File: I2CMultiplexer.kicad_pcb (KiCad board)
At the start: 2 copper layers, 165.1 x 88.9 mm, 178 parts, among them J1 M3, J10 I2C, J11 I2C, J12 I2C, J13 RSS232Out, J14 RSS232In, J15 SPI, J16 SPI, J17 V_{IN}, J18 UART8, J19 UART5, J2 M3, J20 UART6, J3 M3, J4 M3, J5 I2C, J6 I2C, J7 I2C, J8 I2C, J9 I2C, Q1 Q_PMOS_GSD, Q2 Q_PMOS_GSD, U1 Teensy4.1, U2 TCA9548APWR, U3 PCF8574TS, U4 MAX3232, U5 FM24CL16B

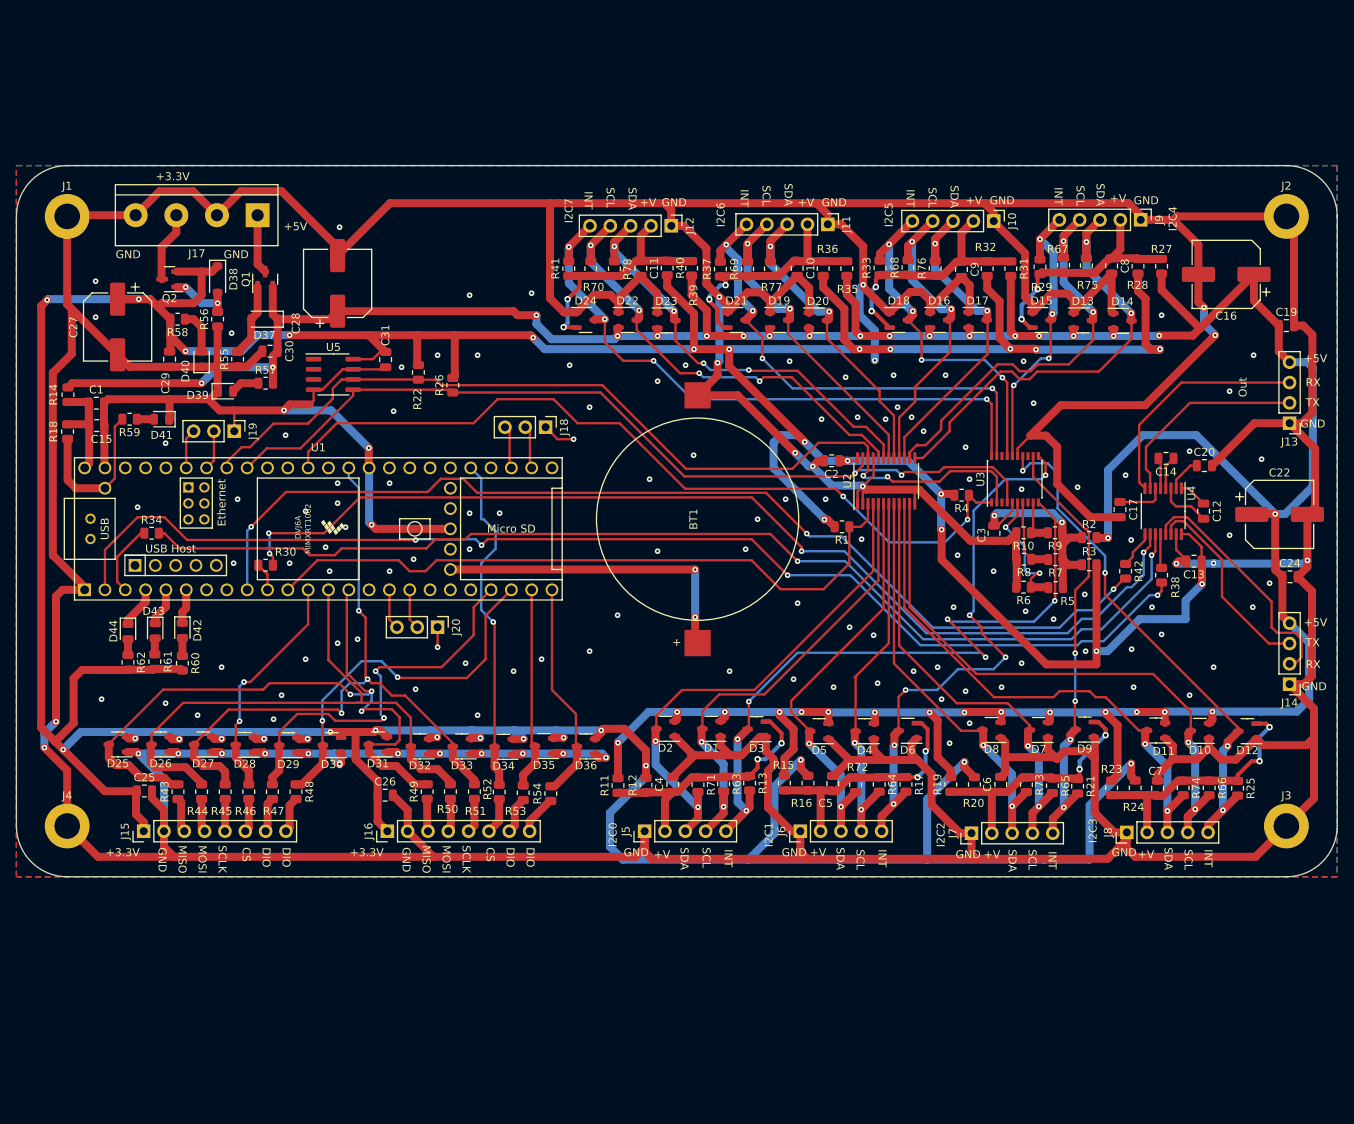
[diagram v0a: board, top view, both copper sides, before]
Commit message: Start layout. Swap side for connectors.
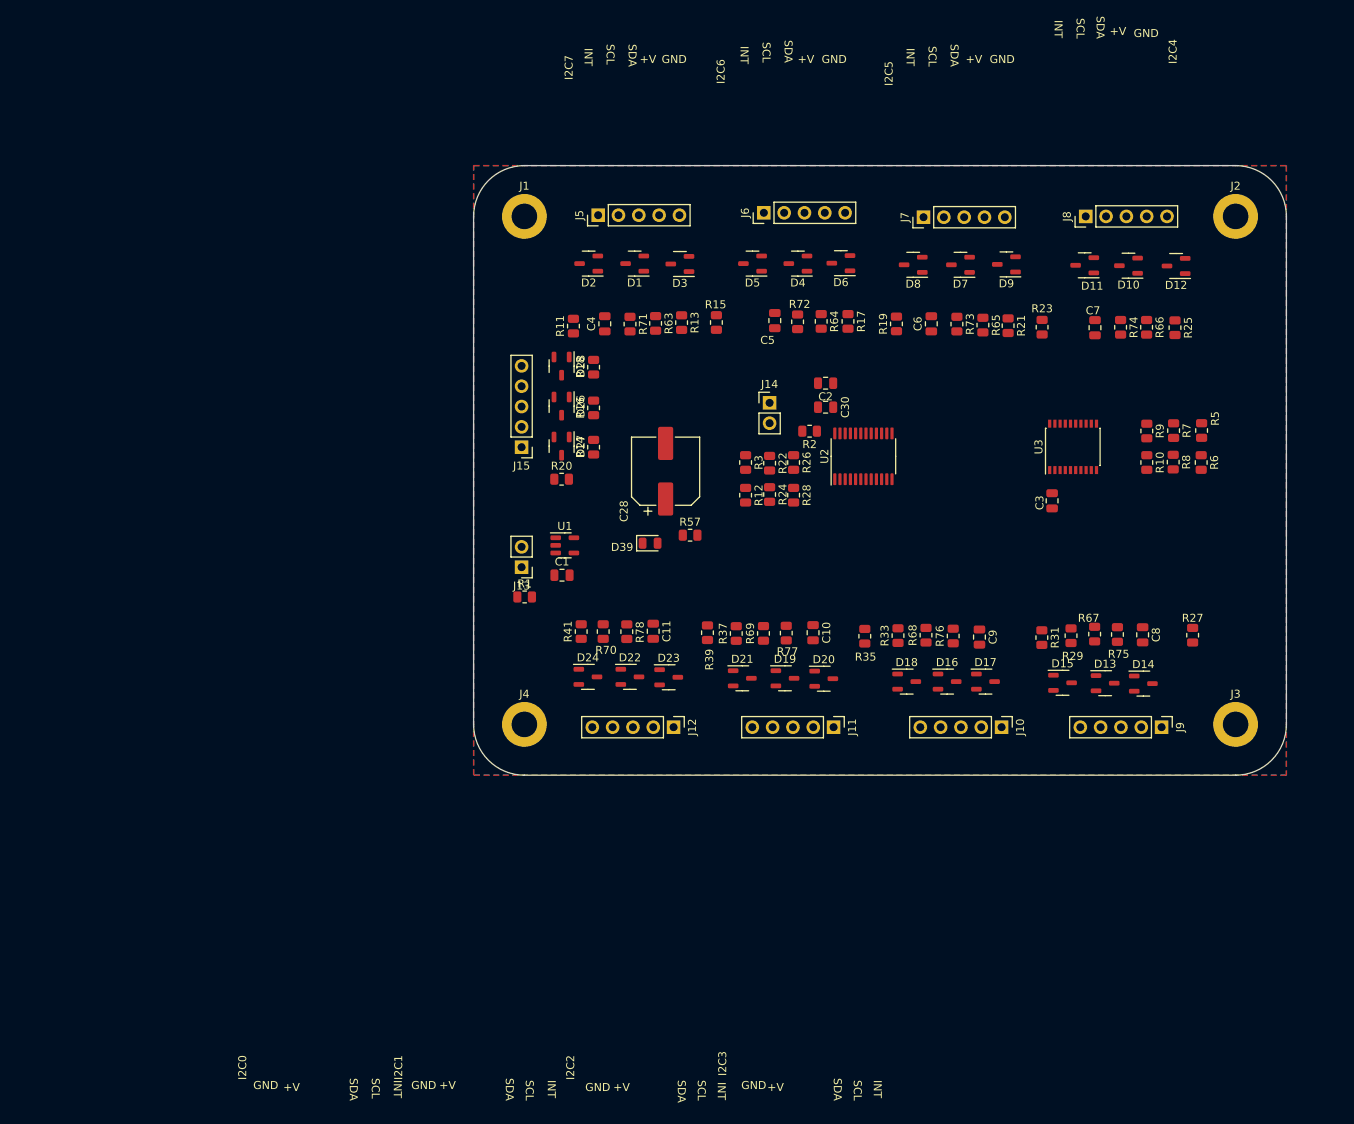
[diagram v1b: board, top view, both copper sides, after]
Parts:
- removed BT1: 2032Coin, BatteryCoin:BC2032
- removed C12, C13, C14, C17, C19, C20, C24, C25, C26, C29, C31: 1uF, Capacitor_SMD:C_0805_2012Metric
- removed C15: 10uF, Capacitor_SMD:C_0805_2012Metric
- removed C16, C22, C27: 100uF, Capacitor_SMD:CP_Elec_8x11.9
- removed D25, D29, D30, D31, D32, D33, D34, D35, D36: 100V, Package_TO_SOT_SMD:SOT-23-3
- removed D37, D38: 10V, Diode_SMD:D_SOD-123
- removed D40, D41, D42, D43, D44: LED, LED_SMD:LED_0805_2012Metric
- removed J16: SPI, Connector_PinHeader_2.54mm:PinHeader_1x08_P2.54mm_Vertical
- removed J17: V_{IN}, TerminalBlock:TerminalBlock_bornier-4_P5.08mm
- removed J18: UART8, Connector_PinHeader_2.54mm:PinHeader_1x03_P2.54mm_Vertical
- removed J19: UART5, Connector_PinHeader_2.54mm:PinHeader_1x03_P2.54mm_Vertical
- removed J20: UART6, Connector_PinHeader_2.54mm:PinHeader_1x03_P2.54mm_Vertical
- removed Q1, Q2: Q_PMOS_GSD, Package_TO_SOT_SMD:SOT-23
- removed R30, R34, R38, R42, R59, R60, R61, R62: 500Ω, Resistor_SMD:R_0805_2012Metric
- removed R32, R36, R40: 0Ω, Resistor_SMD:R_0805_2012Metric
- removed R4: 10kΩ, Resistor_SMD:R_0805_2012Metric
- removed R43, R44, R45, R46, R47, R48, R49, R50, R51, R52, R53, R54: 50Ω, Resistor_SMD:R_0805_2012Metric
- removed R55, R56: 100kΩ, Resistor_SMD:R_0805_2012Metric
- removed R58: 330kΩ, Resistor_SMD:R_0805_2012Metric
- removed U4: MAX3232, Package_SO:TSSOP-16_4.4x5mm_P0.65mm
- removed U5: FM24CL16B, Package_SO:SOIC-8_3.9x4.9mm_P1.27mm
- J13: value RSS232Out -> V_{IN}; footprint Connector_PinHeader_2.54mm:PinHeader_1x04_P2.54mm_Vertical -> Connector_PinHeader_2.54mm:PinHeader_1x02_P2.54mm_Vertical
- J14: value RSS232In -> ~{RESET}; footprint Connector_PinHeader_2.54mm:PinHeader_1x04_P2.54mm_Vertical -> Connector_PinHeader_2.54mm:PinHeader_1x02_P2.54mm_Vertical
- J15: value SPI -> I2C; footprint Connector_PinHeader_2.54mm:PinHeader_1x08_P2.54mm_Vertical -> Connector_PinHeader_2.54mm:PinHeader_1x05_P2.54mm_Vertical
- R1: value 10kΩ -> 100kΩ
- R12, R14, R16, R18, R2, R24, R28, R3: value 0Ω -> 10kΩ
- R20: value 0Ω -> NS
- U1: value Teensy4.1 -> MAX40200AUK; footprint Teensy:Teensy41 -> Package_TO_SOT_SMD:SOT-23-5
- moved J13 97.7 mm to (133.0, 101.0)
- moved J6 77.4 mm to (163.3, 56.7)
- moved J7 77.2 mm to (183.2, 57.2)
- moved J5 77.2 mm to (142.6, 57.0)
- moved J8 77.2 mm to (203.5, 57.1)
- moved J14 73.9 mm to (164.0, 80.5), turned to 0 degrees
- moved C30 69.8 mm to (171.0, 81.0)
- moved J15 67.3 mm to (133.0, 86.0), turned to 180 degrees
- moved R18 66.2 mm to (142.0, 76.0), turned to 90 degrees
- moved R14 66.0 mm to (142.0, 86.0), turned to 90 degrees
- moved D26 65.6 mm to (138.0, 80.9), turned to -90 degrees
- moved R20 64.2 mm to (138.0, 90.0), turned to 0 degrees
- moved J9 63.5 mm to (213.0, 121.0)
- moved J10 63.3 mm to (193.0, 121.0)
- moved J11 62.9 mm to (172.0, 121.0)
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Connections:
- C1 pad 1: Net-(U1-VIN) -> Net-(U1-EN)
- C2 pad 1: +3.3V -> +5V
- C3 pad 1: Net-(U3-VDD) -> +5V
- D12 pad 2: /TCA9548AI2CMultiplexer/I2CConnector3/VBus -> +5V
- D15 pad 2: /TCA9548AI2CMultiplexer/I2CConnector4/VBus -> +5V
- D18 pad 2: /TCA9548AI2CMultiplexer/I2CConnector5/VBus -> +5V
- D21 pad 2: /TCA9548AI2CMultiplexer/I2CConnector6/VBus -> +5V
- D24 pad 2: /TCA9548AI2CMultiplexer/I2CConnector7/VBus -> +5V
- D26 pad 2: +3.3V -> +5V
- D26 pad 3: /MOSI -> /I2CInput/SDA
- D27 pad 2: +3.3V -> +5V
- D27 pad 3: /SCLK -> /I2CInput/SCL
- D28 pad 2: +3.3V -> +5V
- D28 pad 3: /CS0 -> /I2CInput/INT
- D3 pad 2: /TCA9548AI2CMultiplexer/I2CConnector/VBus -> +5V
- D6 pad 2: /TCA9548AI2CMultiplexer/I2CConnector1/VBus -> +5V
- D9 pad 2: /TCA9548AI2CMultiplexer/I2CConnector2/VBus -> +5V
- J15 pad 1: +3.3V -> GND
- J15 pad 2: GND -> /I2CInput/VI2C
- J15 pad 3: Net-(J15-Pin_3) -> /I2CInput/SDA
- J15 pad 4: Net-(J15-Pin_4) -> /I2CInput/SCL
- J15 pad 5: Net-(J15-Pin_5) -> /I2CInput/INT
- R1 pad 1: /~{RESET}I2C -> Net-(U1-EN)
- R1 pad 2: +3.3V -> Net-(J13-Pin_2)
- R12 pad 1: /TCA9548AI2CMultiplexer/I2CConnector/VBus -> /TCA9548AI2CMultiplexer/A0
- R12 pad 2: +3.3V -> GND
- R14 pad 1: +5V -> /I2CInput/SCL
- R14 pad 2: Net-(U1-VIN) -> /I2CInput/VI2C
- R16 pad 1: /TCA9548AI2CMultiplexer/I2CConnector1/VBus -> /I2CInput/SDA
- R16 pad 2: +3.3V -> /I2CInput/VI2C
- R18 pad 1: Net-(U1-VIN) -> /I2CInput/INT
- R18 pad 2: Net-(U1-VUSB) -> /I2CInput/VI2C
- R2 pad 1: Net-(U3-VDD) -> +5V
- R2 pad 2: +5V -> Net-(J14-Pin_2)
- R20 pad 1: /TCA9548AI2CMultiplexer/I2CConnector2/VBus -> /I2CInput/VI2C
- R20 pad 2: +3.3V -> +5V
- R22 pad 1: /SCL -> +5V
- R22 pad 2: +3.3V -> /TCA9548AI2CMultiplexer/A1
- R24 pad 1: /TCA9548AI2CMultiplexer/I2CConnector3/VBus -> /TCA9548AI2CMultiplexer/A1
- R24 pad 2: +3.3V -> GND
- R26 pad 1: /SDA -> +5V
- R26 pad 2: +3.3V -> /TCA9548AI2CMultiplexer/A2
- R28 pad 1: /TCA9548AI2CMultiplexer/I2CConnector4/VBus -> /TCA9548AI2CMultiplexer/A2
- R28 pad 2: +3.3V -> GND
- R3 pad 1: Net-(U3-VDD) -> +5V
- R3 pad 2: +3.3V -> /TCA9548AI2CMultiplexer/A0
- R5 pad 1: Net-(U3-VDD) -> +5V
- R7 pad 1: Net-(U3-VDD) -> +5V
- R9 pad 1: Net-(U3-VDD) -> +5V
- U1 pad 1: GND -> Net-(J13-Pin_2)
- U1 pad 2: /RX0 -> GND
- U1 pad 3: Net-(U1-1_TX1_CTX2_MISO1) -> Net-(U1-EN)
- U1 pad 4: Net-(D44-K) -> unconnected-(U1-NC-Pad4)
- U1 pad 5: Net-(D43-K) -> +5V
- U2 pad 1: GND -> /TCA9548AI2CMultiplexer/A0
- U2 pad 2: GND -> /TCA9548AI2CMultiplexer/A1
- U2 pad 21: GND -> /TCA9548AI2CMultiplexer/A2
- U2 pad 22: /SCL -> /I2CInput/SCL
- U2 pad 23: /SDA -> /I2CInput/SDA
- U2 pad 24: +3.3V -> +5V
- U2 pad 3: /~{RESET}I2C -> Net-(J14-Pin_2)
- U3 pad 1: /TCA9548AI2CMultiplexer/~{INT} -> /I2CInput/INT
- U3 pad 2: /SCL -> /I2CInput/SCL
- U3 pad 4: /SDA -> /I2CInput/SDA
- U3 pad 5: Net-(U3-VDD) -> +5V
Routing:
- net GND: track 1212.6 -> 0.00 mm, vias 141 -> 0
- net +3.3V: track 694.0 -> 0.00 mm, vias 36 -> 0
- net +5V: track 441.7 -> 0.00 mm, vias 35 -> 0
- net /RX0: track 150.0 -> 0.00 mm, vias 4 -> 0
- net /TX0: track 140.8 -> 0.00 mm, vias 2 -> 0
- net /TX1: track 131.2 -> 0.00 mm, vias 4 -> 0
- net /RX1: track 130.1 -> 0.00 mm, vias 3 -> 0
- net /SCL: track 117.1 -> 0.00 mm, vias 2 -> 0
- net /SDA: track 110.7 -> 0.00 mm, vias 2 -> 0
- net /TCA9548AI2CMultiplexer/~{INT}: track 102.1 -> 0.00 mm, vias 2 -> 0
- net /MISO: track 88.2 -> 0.00 mm, vias 3 -> 0
- net /TCA9548AI2CMultiplexer/I2CConnector/INT: track 87.8 -> 0.00 mm, vias 6 -> 0
- net /~{RESET}I2C: track 84.9 -> 0.00 mm
- net /SCLK: track 82.5 -> 0.00 mm, vias 3 -> 0
- net /TCA9548AI2CMultiplexer/I2CConnector7/INT: track 78.7 -> 0.00 mm, vias 4 -> 0
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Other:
- board size 165.1 x 88.9 mm -> 101.6 x 76.2 mm
- board text removed: "+3.3V"
- board text removed: "+5V"
- board text removed: "CS"
- board text removed: "DIO"
- board text removed: "MISO"
- board text removed: "MOSI"
- board text removed: "Out"
- board text removed: "RX"
- board text removed: "SCLK"
- board text removed: "TX"

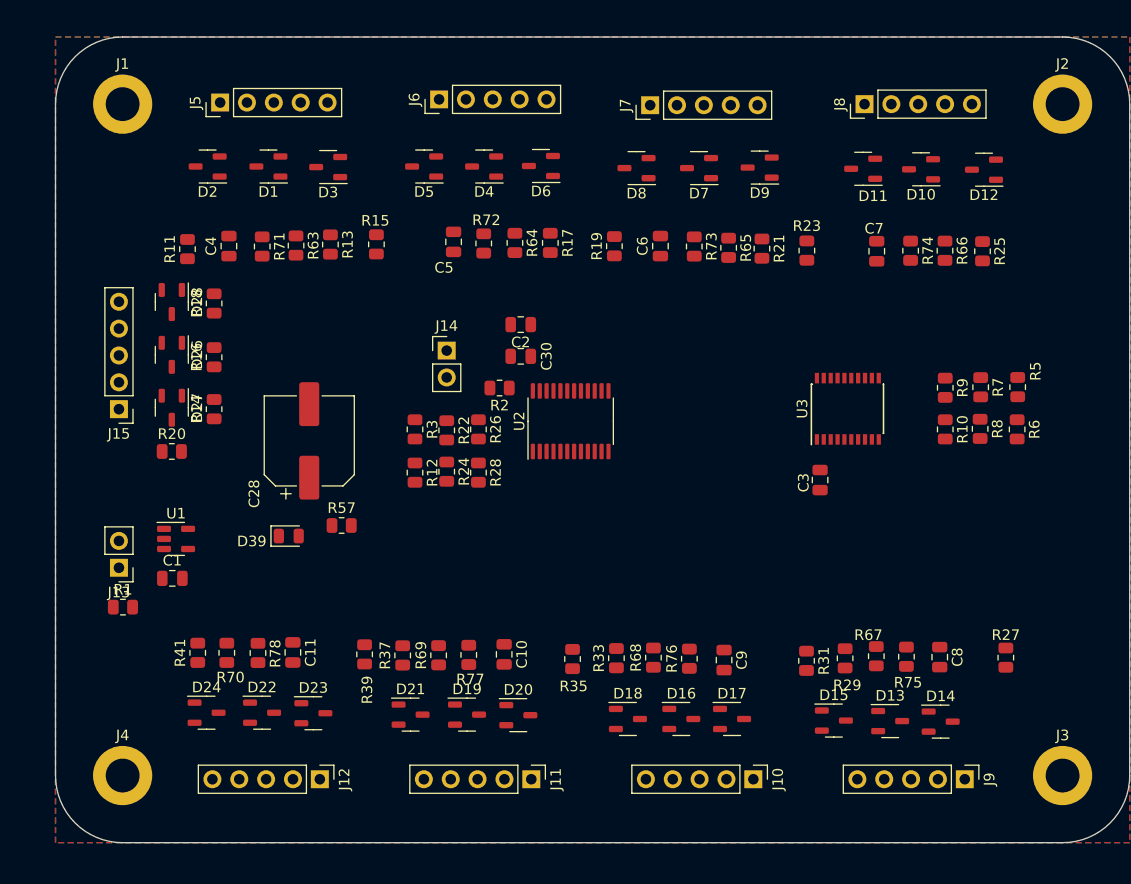
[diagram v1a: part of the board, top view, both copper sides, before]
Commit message: Swap I2C connections.
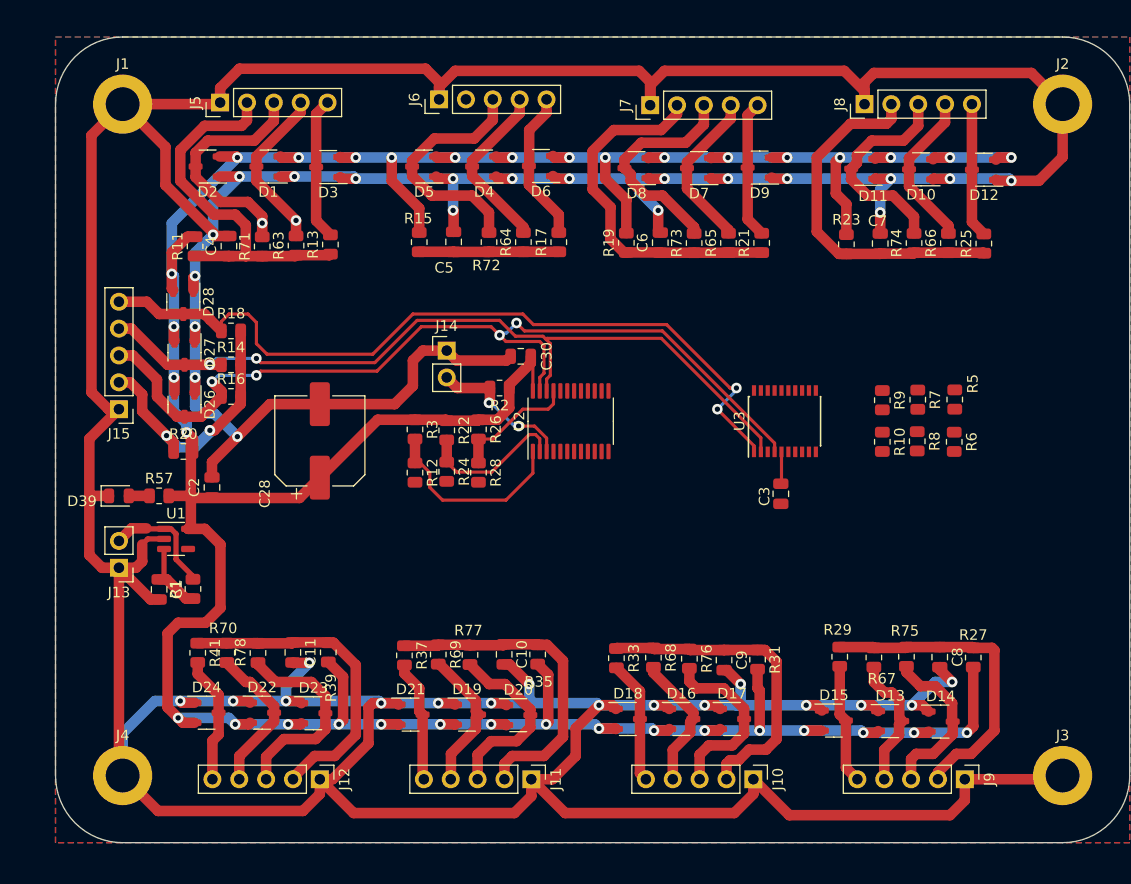
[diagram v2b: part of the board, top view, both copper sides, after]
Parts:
- moved C2 33.0 mm to (141.8, 93.4), turned to 90 degrees
- moved R57 17.5 mm to (136.8, 94.2)
- moved D39 16.5 mm to (133.0, 94.2)
- moved R1 6.84 mm to (140.0, 103.0), turned to 90 degrees
- moved R10 6.06 mm to (205.2, 89.1)
- moved R9 6.06 mm to (205.2, 85.2)
- moved R5 6.06 mm to (212.1, 85.1)
- moved R6 6.06 mm to (212.0, 89.1)
- moved R7 6.06 mm to (208.6, 85.1)
- moved R8 6.06 mm to (208.5, 89.0)
- moved U3 6.06 mm to (196.0, 87.1)
- moved D27 5.34 mm to (139.2, 80.7)
- moved D26 4.86 mm to (139.2, 85.6)
- moved R31 4.63 mm to (193.4, 109.7)
- moved R14 4.49 mm to (143.6, 81.8), turned to 0 degrees
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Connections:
- U2 pad 10: /TCA9548AI2CMultiplexer/I2CConnector3/SDA -> /TCA9548AI2CMultiplexer/I2CConnector4/SDA
- U2 pad 11: /TCA9548AI2CMultiplexer/I2CConnector3/SCL -> /TCA9548AI2CMultiplexer/I2CConnector4/SCL
- U2 pad 13: /TCA9548AI2CMultiplexer/I2CConnector4/SDA -> /TCA9548AI2CMultiplexer/I2CConnector3/SDA
- U2 pad 14: /TCA9548AI2CMultiplexer/I2CConnector4/SCL -> /TCA9548AI2CMultiplexer/I2CConnector3/SCL
- U2 pad 15: /TCA9548AI2CMultiplexer/I2CConnector5/SDA -> /TCA9548AI2CMultiplexer/I2CConnector2/SDA
- U2 pad 16: /TCA9548AI2CMultiplexer/I2CConnector5/SCL -> /TCA9548AI2CMultiplexer/I2CConnector2/SCL
- U2 pad 17: /TCA9548AI2CMultiplexer/I2CConnector6/SDA -> /TCA9548AI2CMultiplexer/I2CConnector1/SDA
- U2 pad 18: /TCA9548AI2CMultiplexer/I2CConnector6/SCL -> /TCA9548AI2CMultiplexer/I2CConnector1/SCL
- U2 pad 19: /TCA9548AI2CMultiplexer/I2CConnector7/SDA -> /TCA9548AI2CMultiplexer/I2CConnector/SDA
- U2 pad 20: /TCA9548AI2CMultiplexer/I2CConnector7/SCL -> /TCA9548AI2CMultiplexer/I2CConnector/SCL
- U2 pad 4: /TCA9548AI2CMultiplexer/I2CConnector/SDA -> /TCA9548AI2CMultiplexer/I2CConnector7/SDA
- U2 pad 5: /TCA9548AI2CMultiplexer/I2CConnector/SCL -> /TCA9548AI2CMultiplexer/I2CConnector7/SCL
- U2 pad 6: /TCA9548AI2CMultiplexer/I2CConnector1/SDA -> /TCA9548AI2CMultiplexer/I2CConnector6/SDA
- U2 pad 7: /TCA9548AI2CMultiplexer/I2CConnector1/SCL -> /TCA9548AI2CMultiplexer/I2CConnector6/SCL
- U2 pad 8: /TCA9548AI2CMultiplexer/I2CConnector2/SDA -> /TCA9548AI2CMultiplexer/I2CConnector5/SDA
- U2 pad 9: /TCA9548AI2CMultiplexer/I2CConnector2/SCL -> /TCA9548AI2CMultiplexer/I2CConnector5/SCL
- U3 pad 10: /TCA9548AI2CMultiplexer/I2CConnector/INT -> /TCA9548AI2CMultiplexer/I2CConnector7/INT
- U3 pad 11: /TCA9548AI2CMultiplexer/I2CConnector1/INT -> /TCA9548AI2CMultiplexer/I2CConnector6/INT
- U3 pad 12: /TCA9548AI2CMultiplexer/I2CConnector2/INT -> /TCA9548AI2CMultiplexer/I2CConnector5/INT
- U3 pad 14: /TCA9548AI2CMultiplexer/I2CConnector3/INT -> /TCA9548AI2CMultiplexer/I2CConnector4/INT
- U3 pad 16: /TCA9548AI2CMultiplexer/I2CConnector4/INT -> /TCA9548AI2CMultiplexer/I2CConnector3/INT
- U3 pad 17: /TCA9548AI2CMultiplexer/I2CConnector5/INT -> /TCA9548AI2CMultiplexer/I2CConnector2/INT
- U3 pad 19: /TCA9548AI2CMultiplexer/I2CConnector6/INT -> /TCA9548AI2CMultiplexer/I2CConnector1/INT
- U3 pad 20: /TCA9548AI2CMultiplexer/I2CConnector7/INT -> /TCA9548AI2CMultiplexer/I2CConnector/INT
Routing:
- net GND: track 0.00 -> 641.8 mm, vias 0 -> 36
- net +5V: track 0.00 -> 356.4 mm, vias 0 -> 35
- net /I2CInput/SDA: track 0.00 -> 87.0 mm, vias 0 -> 4
- net /I2CInput/SCL: track 0.00 -> 76.5 mm, vias 0 -> 2
- net /I2CInput/INT: track 0.00 -> 76.2 mm, vias 0 -> 2
- net /TCA9548AI2CMultiplexer/I2CConnector/VBus: track 0.00 -> 35.8 mm
- net /TCA9548AI2CMultiplexer/I2CConnector2/VBus: track 0.00 -> 34.1 mm
- net /TCA9548AI2CMultiplexer/I2CConnector3/VBus: track 0.00 -> 33.7 mm
- net /TCA9548AI2CMultiplexer/I2CConnector6/VBus: track 0.00 -> 31.0 mm
- net /TCA9548AI2CMultiplexer/I2CConnector7/VBus: track 0.00 -> 30.2 mm
- net /TCA9548AI2CMultiplexer/I2CConnector5/VBus: track 0.00 -> 30.2 mm
- net /TCA9548AI2CMultiplexer/I2CConnector4/VBus: track 0.00 -> 30.0 mm
- net /I2CInput/VI2C: track 0.00 -> 25.5 mm, vias 0 -> 2
- net /TCA9548AI2CMultiplexer/I2CConnector1/SDA: track 0.00 -> 23.2 mm
- net /TCA9548AI2CMultiplexer/I2CConnector/SDA: track 0.00 -> 22.5 mm, vias 0 -> 1
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
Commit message: Added labels. Ready for final cleanup and checking.
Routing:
- net GND: track 641.8 -> 753.9 mm, vias 36 -> 74
- net /TCA9548AI2CMultiplexer/I2CConnector7/INT: track 12.1 -> 89.9 mm, vias 0 -> 2
- net /TCA9548AI2CMultiplexer/I2CConnector6/INT: track 11.6 -> 81.7 mm, vias 0 -> 4
- net /TCA9548AI2CMultiplexer/I2CConnector7/SCL: track 14.5 -> 68.5 mm, vias 0 -> 4
- net /TCA9548AI2CMultiplexer/I2CConnector/INT: track 13.5 -> 66.5 mm, vias 0 -> 2
- net /TCA9548AI2CMultiplexer/I2CConnector4/SDA: track 15.9 -> 66.8 mm, vias 0 -> 4
- net /TCA9548AI2CMultiplexer/I2CConnector7/SDA: track 19.7 -> 68.1 mm, vias 0 -> 4
- net /TCA9548AI2CMultiplexer/I2CConnector4/SCL: track 12.8 -> 60.3 mm, vias 0 -> 4
- net /TCA9548AI2CMultiplexer/I2CConnector3/SCL: track 15.2 -> 61.9 mm, vias 0 -> 4
- net +5V: track 356.4 -> 402.3 mm, vias 35 -> 39
- net /TCA9548AI2CMultiplexer/I2CConnector/SDA: track 22.5 -> 66.5 mm, vias 1 -> 4
- net /TCA9548AI2CMultiplexer/I2CConnector3/SDA: track 20.5 -> 64.0 mm, vias 0 -> 4
- net /TCA9548AI2CMultiplexer/I2CConnector/SCL: track 15.9 -> 55.1 mm, vias 1 -> 4
- net /TCA9548AI2CMultiplexer/I2CConnector5/INT: track 11.7 -> 50.5 mm, vias 0 -> 4
- net /TCA9548AI2CMultiplexer/I2CConnector6/SCL: track 13.7 -> 50.1 mm, vias 0 -> 4
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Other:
- board text added: "PCF8574TS"
- board text added: "RESET"
- board text added: "TCA9548APWR"
- board text added: "V_{IN}"
